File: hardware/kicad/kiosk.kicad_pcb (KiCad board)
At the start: 2 copper layers, 170 x 116 mm, 15 parts, among them J10 TerminalBlock_MaiXu_MX126-5.0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, J11 TerminalBlock_MaiXu_MX126-5.0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, J13 PinHeader_1x09_P2.54mm_Vertic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, J3 PinSocket_1x14_P2.54mm_Vertic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, J4 PinSocket_1x06_P2.54mm_Vertic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, J5 PinSocket_1x04_P2.54mm_Vertic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, J6 PinSocket_1x06_P2.54mm_Vertic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, J7 PinSocket_1x07_P2.54mm_Vertic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, J9 PinHeader_1x03_P2.54mm_Vertic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, U1 ESP32-S3-CAM

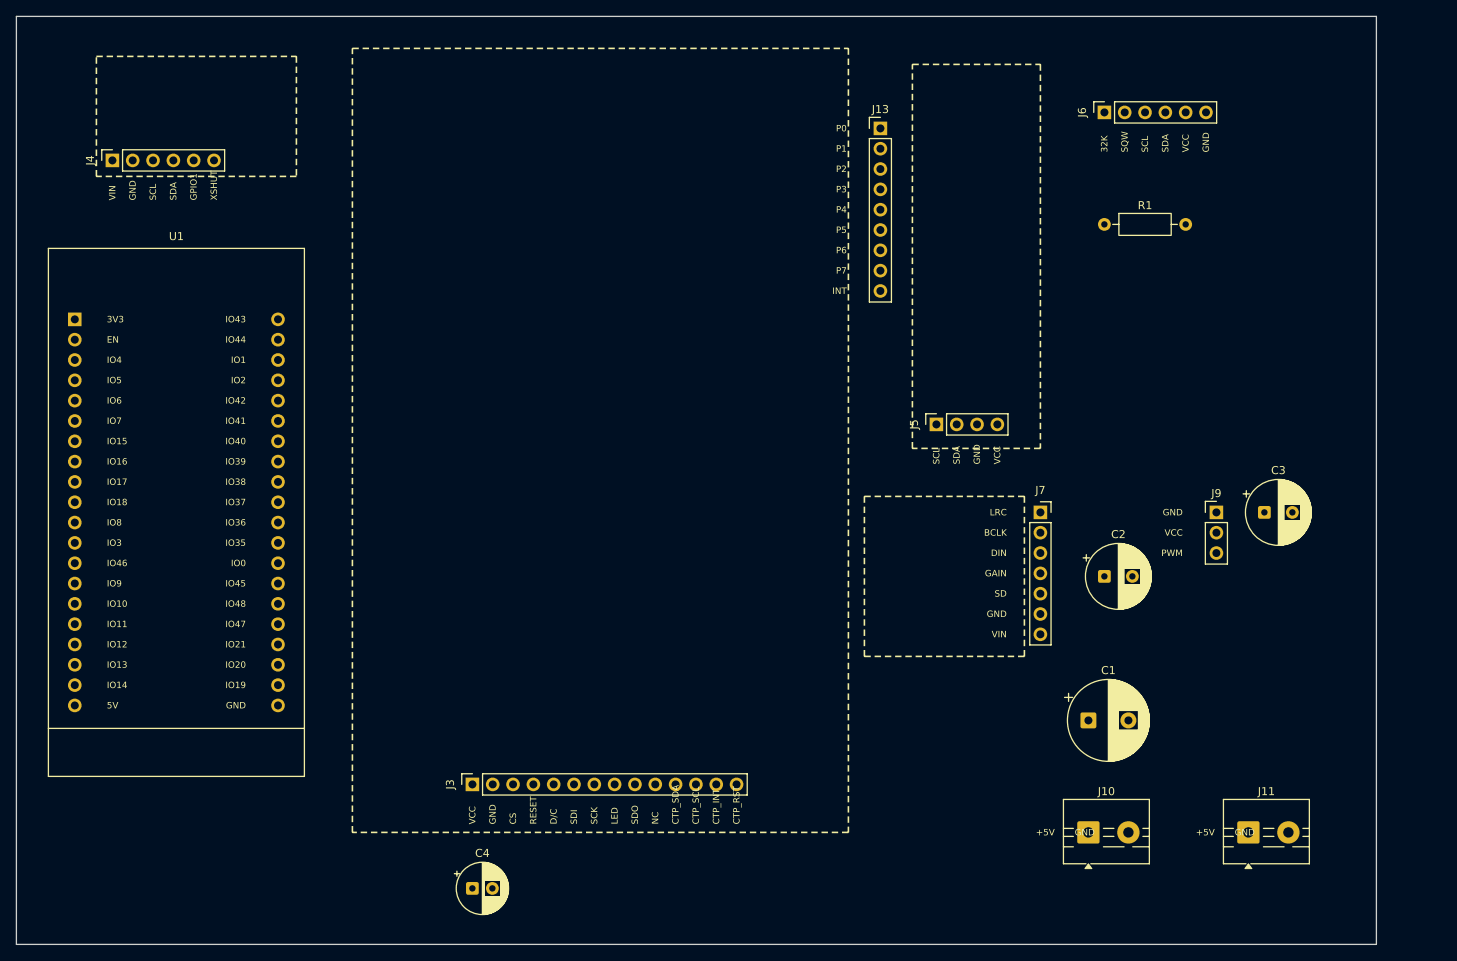
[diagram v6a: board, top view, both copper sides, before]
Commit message: fix(hardware): undo the amplifier flip, centre the ToF, line up the supplies
Moving J7 to the other edge of the amplifier's outline was mine, not a
fact about the part, and it was wrong twice over: the row sits where the
module's header sits, and putting the body on the other side means the
module turned round, which reverses the pin order I left alone. J7 goes
back to the left edge and C2 drops below the outline instead, 8.8 mm from
the VIN pin it decouples.

The ToF header sat against one end of its module instead of centred
between the mounting holes. Six millimetres each side now.

Both supply terminals line up with the panel's capacitor along the bottom
edge.

Pin labels were justified so rotated text grew back over its own pads -
six of them sat on copper. They grow away from the pad now, which leaves
two, both against an outline rather than a pad.
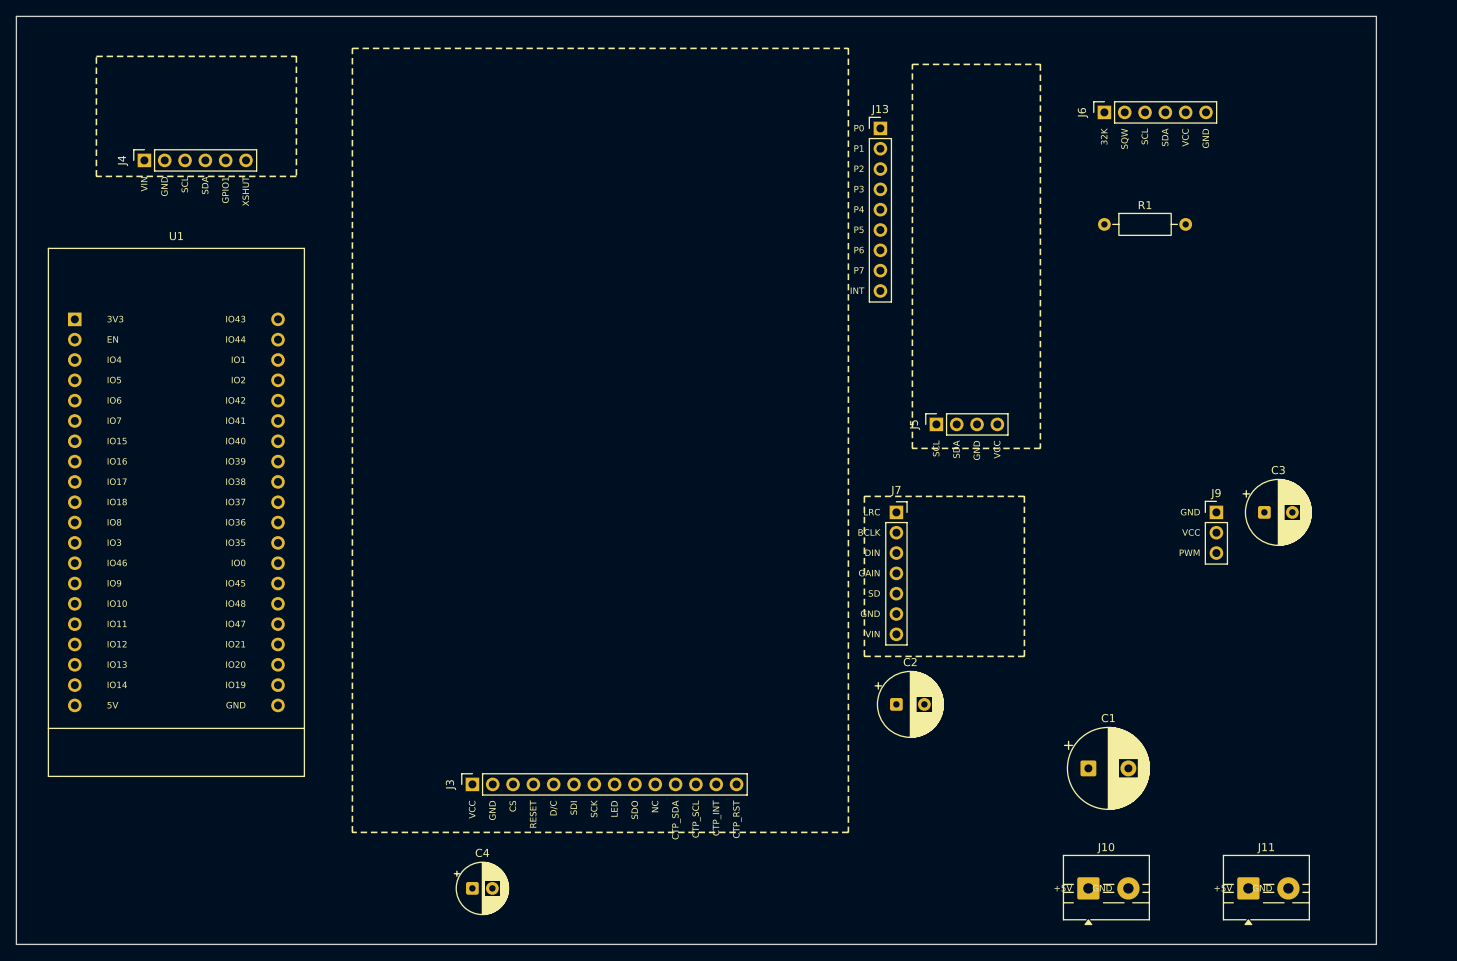
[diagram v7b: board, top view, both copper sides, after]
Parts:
- moved C2 30.5 mm to (110.0, 86.0)
- moved J7 18.0 mm to (110.0, 62.0)
- moved J10 7.00 mm to (134.0, 109.0)
- moved J11 7.00 mm to (154.0, 109.0)
- moved C1 6.00 mm to (134.0, 94.0)
- moved J4 4.00 mm to (16.0, 18.0)

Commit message: fix(hardware): centre the ToF over the devkit and its capacitor on the servo
Both were out by the same 2.5 mm, and both for the same reason: I had
been placing parts by clearing the last collision rather than measuring
against what they sit beside.

The ToF's outline is now centred on the devkit's pin columns, which is
where it belongs since the camera between them is what it points past.
C3 is centred on the servo header it decouples rather than sitting above
it.

Measured after moving, not judged from the render: both read 0.0 mm.
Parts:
- moved C3 2.50 mm to (156.0, 64.5)
- moved J4 2.50 mm to (13.5, 18.0)
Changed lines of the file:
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@@
 	(footprint "Connector_PinSocket_2.54mm:PinSocket_1x06_P2.54mm_Vertical"
 		(layer "F.Cu")
-		(at 16 18 90)
+		(at 13.5 18 90)
 		(descr "Through hole straight socket strip, 1x06, 2.54mm pitch, single row (from Kicad 4.0.7), script generated")
 		(tags "Through hole socket strip THT 1x06 2.54mm single row")
@@
 	(footprint "Capacitor_THT:CP_Radial_D8.0mm_P3.50mm"
 		(layer "F.Cu")
-		(at 156 62)
+		(at 156 64.5)
 		(descr "CP, Radial series, Radial, pin pitch=3.50mm, diameter=8mm, height=12mm, Electrolytic Capacitor")
 		(tags "CP Radial series Radial pin pitch 3.50mm diameter 8mm height 12mm Electrolytic Capacitor")
@@
 	)
 	(gr_line
-		(start 10 5)
-		(end 35 5)
+		(start 7.5 5)
+		(end 32.5 5)
 		(stroke
 			(width 0.2)
@@
 	)
 	(gr_line
-		(start 10 20)
-		(end 10 5)
+		(start 7.5 20)
+		(end 7.5 5)
 		(stroke
 			(width 0.2)
@@
 	)
 	(gr_line
-		(start 35 5)
-		(end 35 20)
+		(start 32.5 5)
+		(end 32.5 20)
 		(stroke
 			(width 0.2)
@@
 	)
 	(gr_line
-		(start 35 20)
-		(end 10 20)
+		(start 32.5 20)
+		(end 7.5 20)
 		(stroke
 			(width 0.2)
@@
 	)
 	(gr_text "VIN"
-		(at 16 20 90)
+		(at 13.5 20 90)
 		(layer "F.SilkS")
 		(effects
@@
 	)
 	(gr_text "GND"
-		(at 18.54 20 90)
+		(at 16.04 20 90)
 		(layer "F.SilkS")
 		(effects
@@
 	)
 	(gr_text "SCL"
-		(at 21.08 20 90)
+		(at 18.58 20 90)
 		(layer "F.SilkS")
 		(effects
@@
 	)
 	(gr_text "SDA"
-		(at 23.62 20 90)
+		(at 21.12 20 90)
 		(layer "F.SilkS")
 		(effects
@@
 	)
 	(gr_text "GPIO1"
-		(at 26.16 20 90)
+		(at 23.66 20 90)
 		(layer "F.SilkS")
 		(effects
@@
 	)
 	(gr_text "XSHUT"
-		(at 28.7 20 90)
+		(at 26.2 20 90)
 		(layer "F.SilkS")
 		(effects
